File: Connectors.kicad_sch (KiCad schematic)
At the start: 4 parts

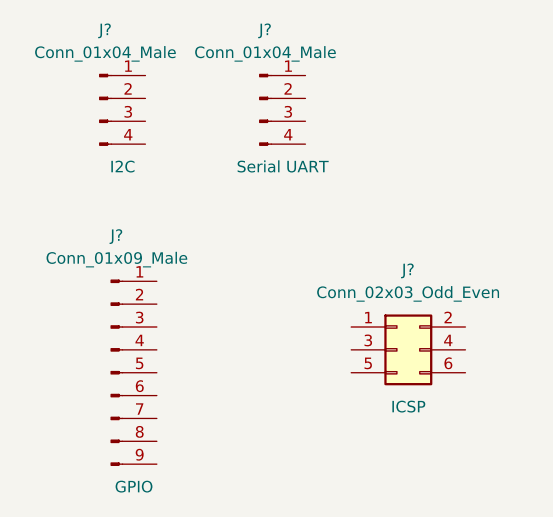
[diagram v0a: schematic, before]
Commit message: changed locations of symbols
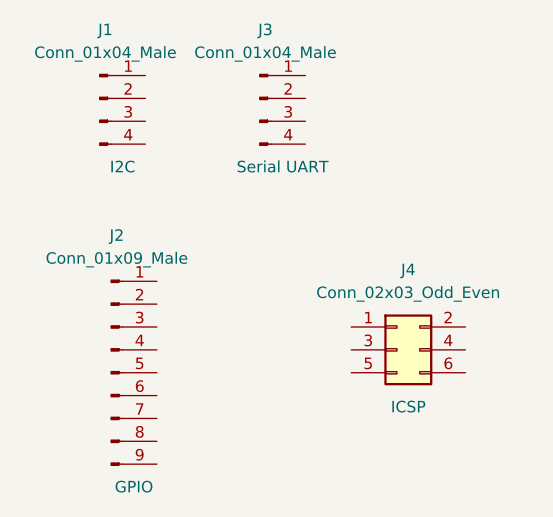
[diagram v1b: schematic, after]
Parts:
- gave numbers to parts that had none: 4
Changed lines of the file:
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@@
   (symbol (lib_id "Connector_Generic:Conn_02x03_Odd_Even") (at 161.29 121.92 0) (unit 1)
     (in_bom yes) (on_board yes)
-    (property "Reference" "J?" (id 0) (at 162.56 113.03 0))
+    (property "Reference" "J4" (id 0) (at 162.56 113.03 0))
     (property "Value" "Conn_02x03_Odd_Even" (id 1) (at 162.56 115.57 0))
     (property "Footprint" "" (id 2) (at 161.29 121.92 0)
@@
   (symbol (lib_id "Connector:Conn_01x09_Male") (at 129.54 124.46 0) (unit 1)
     (in_bom yes) (on_board yes)
-    (property "Reference" "J?" (id 0) (at 130.175 109.22 0))
+    (property "Reference" "J2" (id 0) (at 130.175 109.22 0))
     (property "Value" "Conn_01x09_Male" (id 1) (at 130.175 111.76 0))
     (property "Footprint" "" (id 2) (at 129.54 124.46 0)
@@
   (symbol (lib_id "Connector:Conn_01x04_Male") (at 128.27 93.98 0) (unit 1)
     (in_bom yes) (on_board yes)
-    (property "Reference" "J?" (id 0) (at 128.905 86.36 0))
+    (property "Reference" "J1" (id 0) (at 128.905 86.36 0))
     (property "Value" "Conn_01x04_Male" (id 1) (at 128.905 88.9 0))
     (property "Footprint" "" (id 2) (at 128.27 93.98 0)
@@
   (symbol (lib_id "Connector:Conn_01x04_Male") (at 146.05 93.98 0) (unit 1)
     (in_bom yes) (on_board yes)
-    (property "Reference" "J?" (id 0) (at 146.685 86.36 0))
+    (property "Reference" "J3" (id 0) (at 146.685 86.36 0))
     (property "Value" "Conn_01x04_Male" (id 1) (at 146.685 88.9 0))
     (property "Footprint" "" (id 2) (at 146.05 93.98 0)

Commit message: Completed symbol to footprint associations
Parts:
- J1, J3: footprint (none) -> Connector_PinHeader_2.54mm:PinHeader_1x04_P2.54mm_Vertical
- J2: footprint (none) -> Connector_PinHeader_2.54mm:PinHeader_1x09_P2.54mm_Vertical
- J4: footprint (none) -> Connector_PinHeader_2.54mm:PinHeader_2x03_P2.54mm_Vertical
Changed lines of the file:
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@@
     (property "Reference" "J4" (id 0) (at 162.56 113.03 0))
     (property "Value" "Conn_02x03_Odd_Even" (id 1) (at 162.56 115.57 0))
-    (property "Footprint" "" (id 2) (at 161.29 121.92 0)
+    (property "Footprint" "Connector_PinHeader_2.54mm:PinHeader_2x03_P2.54mm_Vertical" (id 2) (at 161.29 121.92 0)
       (effects (font (size 1.27 1.27)) hide)
     )
@@
     (property "Reference" "J2" (id 0) (at 130.175 109.22 0))
     (property "Value" "Conn_01x09_Male" (id 1) (at 130.175 111.76 0))
-    (property "Footprint" "" (id 2) (at 129.54 124.46 0)
+    (property "Footprint" "Connector_PinHeader_2.54mm:PinHeader_1x09_P2.54mm_Vertical" (id 2) (at 129.54 124.46 0)
       (effects (font (size 1.27 1.27)) hide)
     )
@@
     (property "Reference" "J1" (id 0) (at 128.905 86.36 0))
     (property "Value" "Conn_01x04_Male" (id 1) (at 128.905 88.9 0))
-    (property "Footprint" "" (id 2) (at 128.27 93.98 0)
+    (property "Footprint" "Connector_PinHeader_2.54mm:PinHeader_1x04_P2.54mm_Vertical" (id 2) (at 128.27 93.98 0)
       (effects (font (size 1.27 1.27)) hide)
     )
@@
     (property "Reference" "J3" (id 0) (at 146.685 86.36 0))
     (property "Value" "Conn_01x04_Male" (id 1) (at 146.685 88.9 0))
-    (property "Footprint" "" (id 2) (at 146.05 93.98 0)
+    (property "Footprint" "Connector_PinHeader_2.54mm:PinHeader_1x04_P2.54mm_Vertical" (id 2) (at 146.05 93.98 0)
       (effects (font (size 1.27 1.27)) hide)
     )

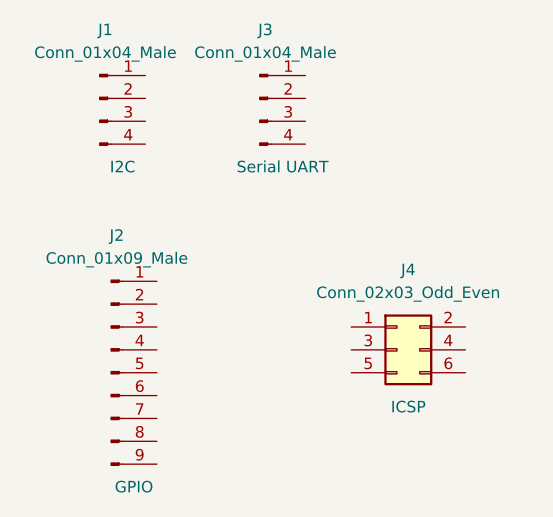
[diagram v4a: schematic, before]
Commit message: Completed wiring in tthe second sheet
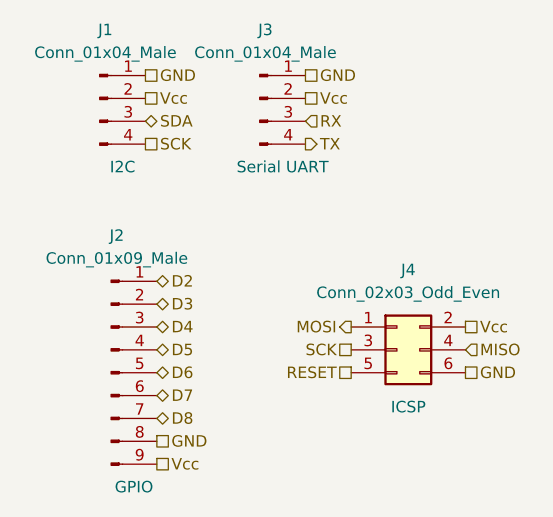
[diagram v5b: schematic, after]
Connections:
- net MOSI: now reaches J4.1 (Pin_1)
- net Vcc: now reaches J4.2 (Pin_2)
- net Vcc: now also J1.2 (Pin_2), J2.9 (Pin_9), J3.2 (Pin_2)
- net SCK: now reaches J4.3 (Pin_3)
- net SCK: now also J1.4 (Pin_4)
- net MISO: now reaches J4.4 (Pin_4)
- net RESET: now reaches J4.5 (Pin_5)
- net GND: now reaches J4.6 (Pin_6)
- net GND: now also J1.1 (Pin_1), J2.8 (Pin_8), J3.1 (Pin_1)
- net D2: now reaches J2.1 (Pin_1)
- net D3: now reaches J2.2 (Pin_2)
- net D4: now reaches J2.3 (Pin_3)
- net D5: now reaches J2.4 (Pin_4)
- net D6: now reaches J2.5 (Pin_5)
- net D7: now reaches J2.6 (Pin_6)
- net D8: now reaches J2.7 (Pin_7)
- net SDA: now reaches J1.3 (Pin_3)
- net RX: now reaches J3.3 (Pin_3)
- net TX: now reaches J3.4 (Pin_4)
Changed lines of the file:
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@@
 (kicad_sch (version 20211123) (generator eeschema)
   (paper "A4")
+  (hierarchical_label "RX" (shape input) (at 151.13 96.52 0)
+    (effects (font (size 1.27 1.27)) (justify left))
+  )
+  (hierarchical_label "D7" (shape bidirectional) (at 134.62 127 0)
+    (effects (font (size 1.27 1.27)) (justify left))
+  )
+  (hierarchical_label "D2" (shape bidirectional) (at 134.62 114.3 0)
+    (effects (font (size 1.27 1.27)) (justify left))
+  )
+  (hierarchical_label "SDA" (shape bidirectional) (at 133.35 96.52 0)
+    (effects (font (size 1.27 1.27)) (justify left))
+  )
+  (hierarchical_label "SCK" (shape passive) (at 156.21 121.92 180)
+    (effects (font (size 1.27 1.27)) (justify right))
+  )
+  (hierarchical_label "D8" (shape bidirectional) (at 134.62 129.54 0)
+    (effects (font (size 1.27 1.27)) (justify left))
+  )
+  (hierarchical_label "GND" (shape passive) (at 133.35 91.44 0)
+    (effects (font (size 1.27 1.27)) (justify left))
+  )
+  (hierarchical_label "Vcc" (shape passive) (at 151.13 93.98 0)
+    (effects (font (size 1.27 1.27)) (justify left))
+  )
+  (hierarchical_label "MOSI" (shape output) (at 156.21 119.38 180)
+    (effects (font (size 1.27 1.27)) (justify right))
+  )
+  (hierarchical_label "MISO" (shape input) (at 168.91 121.92 0)
+    (effects (font (size 1.27 1.27)) (justify left))
+  )
+  (hierarchical_label "GND" (shape passive) (at 168.91 124.46 0)
+    (effects (font (size 1.27 1.27)) (justify left))
+  )
+  (hierarchical_label "TX" (shape output) (at 151.13 99.06 0)
+    (effects (font (size 1.27 1.27)) (justify left))
+  )
+  (hierarchical_label "Vcc" (shape passive) (at 168.91 119.38 0)
+    (effects (font (size 1.27 1.27)) (justify left))
+  )
+  (hierarchical_label "GND" (shape passive) (at 151.13 91.44 0)
+    (effects (font (size 1.27 1.27)) (justify left))
+  )
+  (hierarchical_label "Vcc" (shape passive) (at 133.35 93.98 0)
+    (effects (font (size 1.27 1.27)) (justify left))
+  )
+  (hierarchical_label "GND" (shape passive) (at 134.62 132.08 0)
+    (effects (font (size 1.27 1.27)) (justify left))
+  )
+  (hierarchical_label "SCK" (shape passive) (at 133.35 99.06 0)
+    (effects (font (size 1.27 1.27)) (justify left))
+  )
+  (hierarchical_label "D6" (shape bidirectional) (at 134.62 124.46 0)
+    (effects (font (size 1.27 1.27)) (justify left))
+  )
+  (hierarchical_label "D3" (shape bidirectional) (at 134.62 116.84 0)
+    (effects (font (size 1.27 1.27)) (justify left))
+  )
+  (hierarchical_label "Vcc" (shape passive) (at 134.62 134.62 0)
+    (effects (font (size 1.27 1.27)) (justify left))
+  )
+  (hierarchical_label "D5" (shape bidirectional) (at 134.62 121.92 0)
+    (effects (font (size 1.27 1.27)) (justify left))
+  )
+  (hierarchical_label "D4" (shape bidirectional) (at 134.62 119.38 0)
+    (effects (font (size 1.27 1.27)) (justify left))
+  )
+  (hierarchical_label "RESET" (shape passive) (at 156.21 124.46 180)
+    (effects (font (size 1.27 1.27)) (justify right))
+  )
   (symbol (lib_id "Connector_Generic:Conn_02x03_Odd_Even") (at 161.29 121.92 0) (unit 1)
     (in_bom yes) (on_board yes)
